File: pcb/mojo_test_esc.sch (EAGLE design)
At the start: 1 part

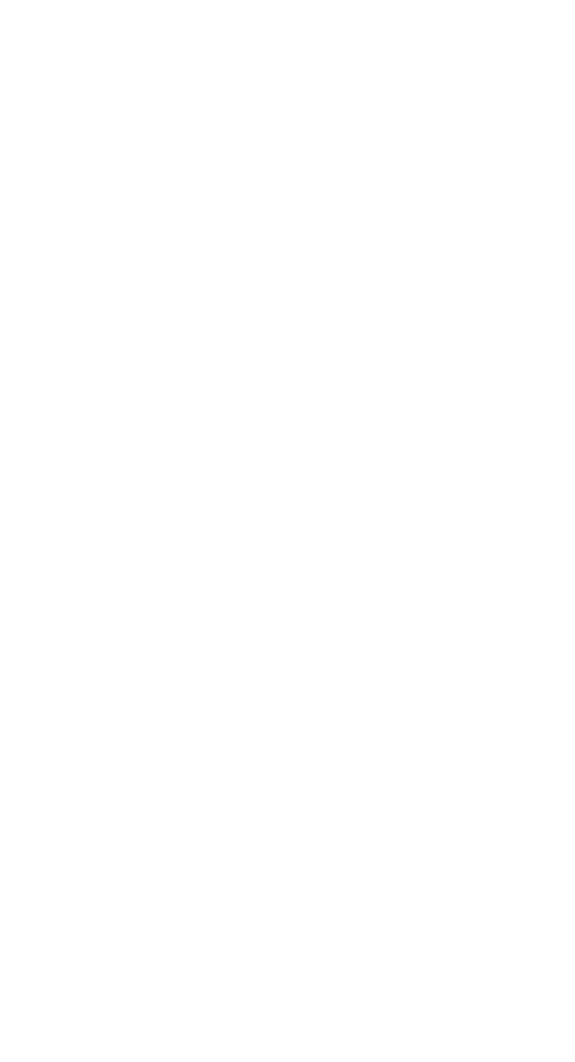
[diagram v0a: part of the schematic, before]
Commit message: Adding D2PAK mosfet to library
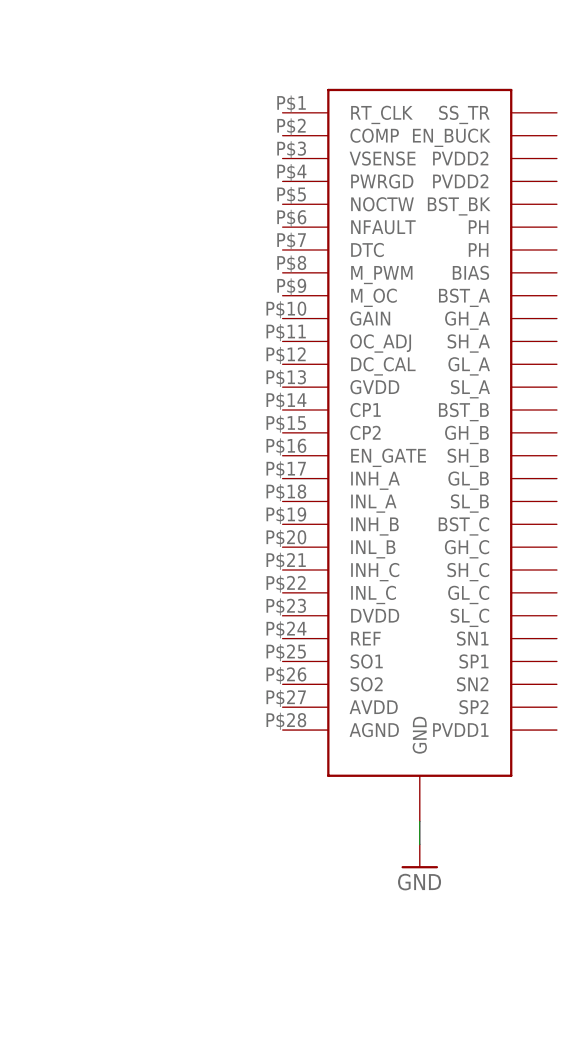
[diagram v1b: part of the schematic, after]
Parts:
- added U$1: DRV8302, mojo_test_esc:DRV8302
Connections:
- new net GND: U$1.GND
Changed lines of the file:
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@@
 <parts>
 <part name="B1" library="mojo_test_esc" deviceset="MOJO_NO_ANALOG" device="V3_NO_LABEL"/>
+<part name="U$1" library="mojo_test_esc" deviceset="DRV8302" device=""/>
+<part name="GND1" library="supply1" deviceset="GND" device=""/>
 </parts>
 <sheets>
@@
 <instance part="B1" gate="G$2" x="-27.94" y="60.96"/>
 <instance part="B1" gate="G$3" x="-27.94" y="-10.16"/>
+<instance part="U$1" gate="G$1" x="53.34" y="50.8"/>
+<instance part="GND1" gate="1" x="53.34" y="2.54"/>
 </instances>
 <busses>
 </busses>
 <nets>
+<net name="GND" class="0">
+<segment>
+<pinref part="U$1" gate="G$1" pin="GND"/>
+<pinref part="GND1" gate="1" pin="GND"/>
+<wire x1="53.34" y1="7.62" x2="53.34" y2="5.08" width="0.1524" layer="91"/>
+</segment>
+</net>
 </nets>
 </sheet>

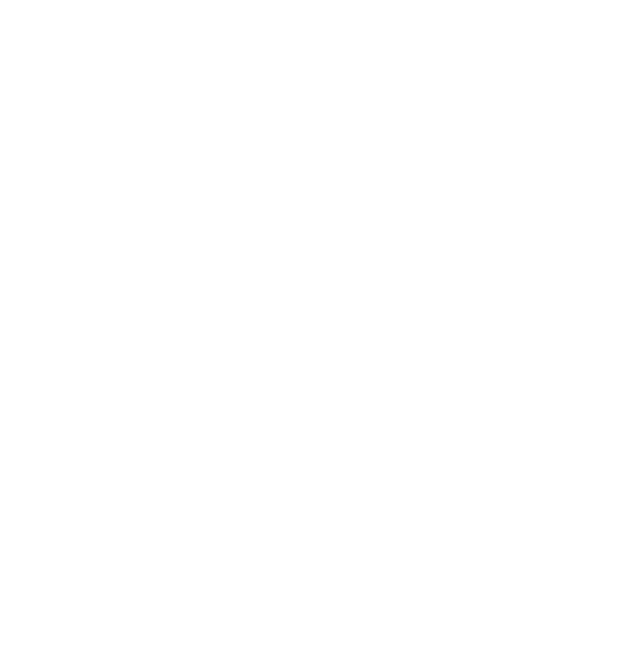
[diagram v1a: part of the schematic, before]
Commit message: Adding SOT23 mosfet packages and associated datasheet
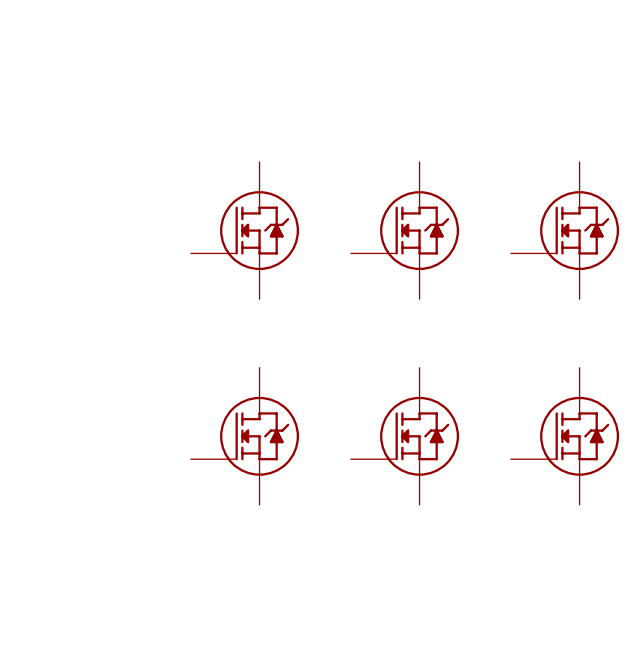
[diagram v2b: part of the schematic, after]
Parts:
- added U$2, U$3, U$4, U$5, U$6, U$7: MOSFETSOT23, mojo_test_esc:MOSFETSOT23
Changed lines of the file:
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@@
 <part name="U$1" library="mojo_test_esc" deviceset="DRV8302" device=""/>
 <part name="GND1" library="supply1" deviceset="GND" device=""/>
+<part name="U$2" library="mojo_test_esc" deviceset="MOSFET" device="SOT23"/>
+<part name="U$3" library="mojo_test_esc" deviceset="MOSFET" device="SOT23"/>
+<part name="U$4" library="mojo_test_esc" deviceset="MOSFET" device="SOT23"/>
+<part name="U$5" library="mojo_test_esc" deviceset="MOSFET" device="SOT23"/>
+<part name="U$6" library="mojo_test_esc" deviceset="MOSFET" device="SOT23"/>
+<part name="U$7" library="mojo_test_esc" deviceset="MOSFET" device="SOT23"/>
 </parts>
 <sheets>
@@
 <instance part="U$1" gate="G$1" x="53.34" y="50.8"/>
 <instance part="GND1" gate="1" x="53.34" y="2.54"/>
+<instance part="U$2" gate="G$1" x="99.06" y="66.04"/>
+<instance part="U$3" gate="G$1" x="116.84" y="66.04"/>
+<instance part="U$4" gate="G$1" x="134.62" y="66.04"/>
+<instance part="U$5" gate="G$1" x="99.06" y="43.18"/>
+<instance part="U$6" gate="G$1" x="116.84" y="43.18"/>
+<instance part="U$7" gate="G$1" x="134.62" y="43.18"/>
 </instances>
 <busses>

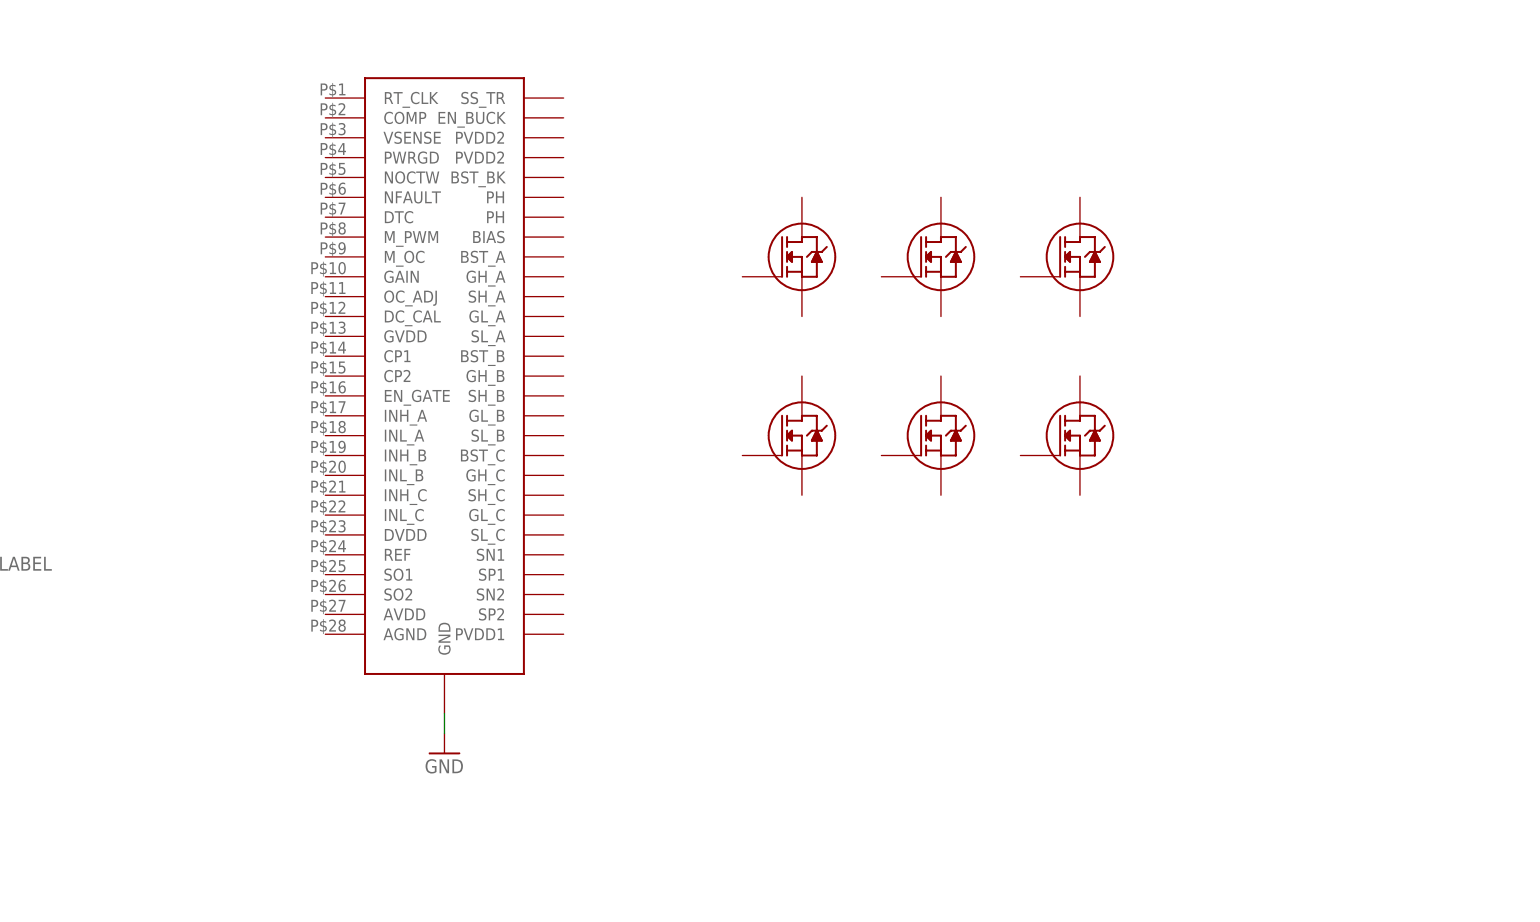
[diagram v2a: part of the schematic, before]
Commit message: Adding 8-pack resistor and updating MOSFETs again
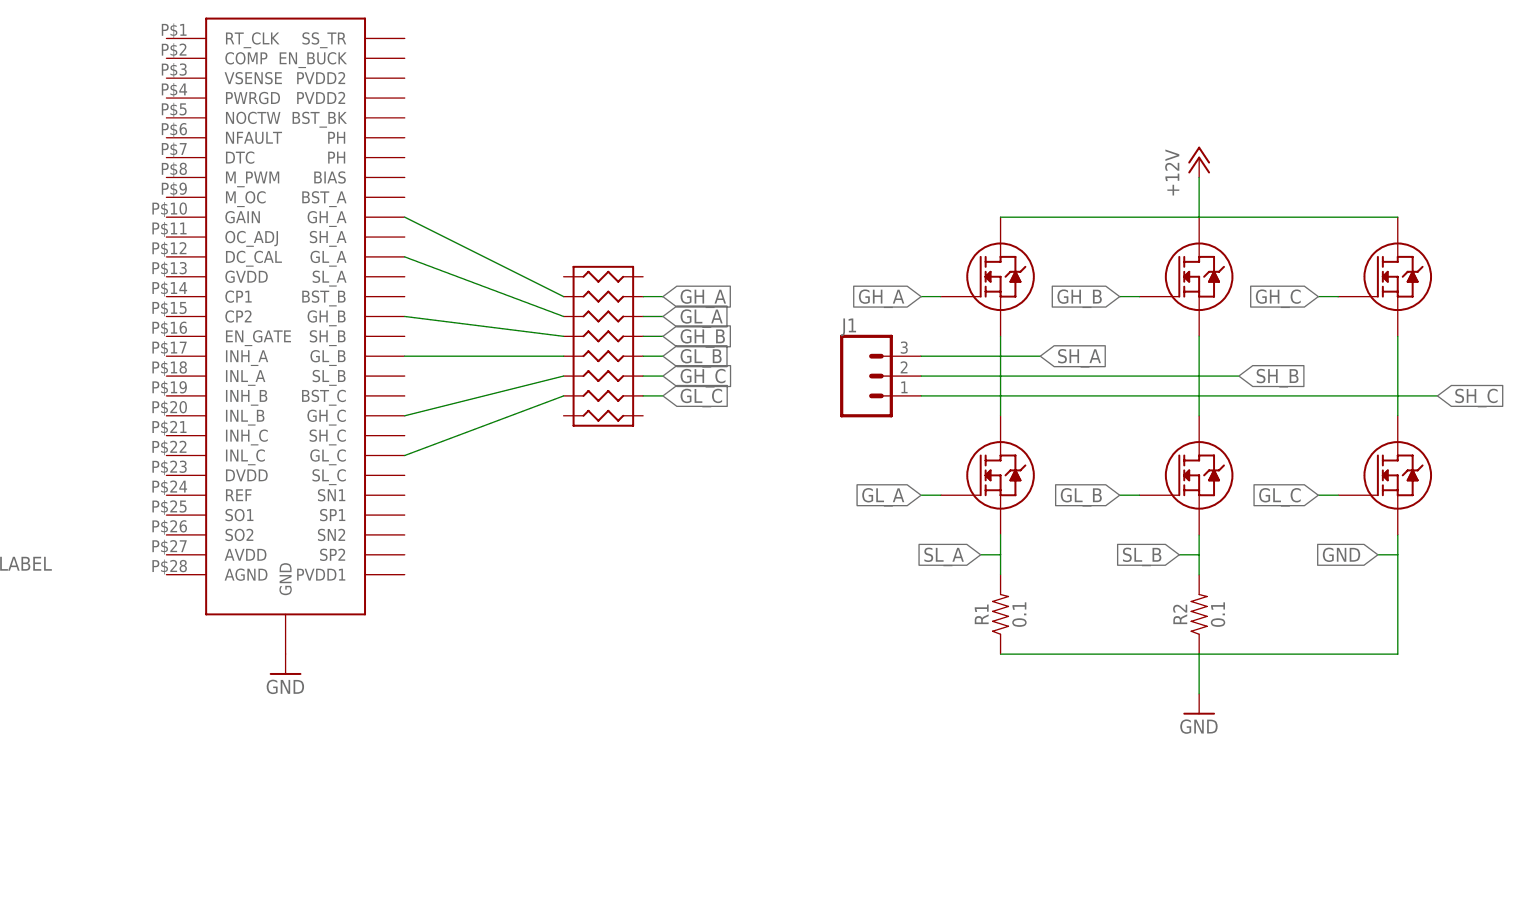
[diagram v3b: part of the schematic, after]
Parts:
- removed U$3, U$4, U$5, U$6, U$7: MOSFETSOT23, mojo_test_esc:MOSFETSOT23
- added J1: (no value), SparkFun-Connectors:CONN_03-SCREW-5MM
- added MOSFET_H_A_1, MOSFET_H_B_1, MOSFET_H_C_1, MOSFET_L_A_1, MOSFET_L_B_1, MOSFET_L_C_1: MOSFET, mojo_test_esc:MOSFET
- added R1, R2: 0.1, SparkFun-Resistors:0.1OHM-1210-1/2W-1%
- U$2: value MOSFETSOT23 -> EXB2HV; device mojo_test_esc:MOSFETSOT23 -> mojo_test_esc:EXB2HV
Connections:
- new net +12V: MOSFET_H_A_1.D2, MOSFET_H_B_1.D2, MOSFET_H_C_1.D2
- new net GH_A: MOSFET_H_A_1.G1, U$2.P2B
- new net GH_B: MOSFET_H_B_1.G1, U$2.P4B
- new net GH_C: MOSFET_H_C_1.G1, U$2.P6B
- new net GL_A: MOSFET_L_A_1.G1, U$2.P3B
- new net GL_B: MOSFET_L_B_1.G1, U$2.P5B
- new net GL_C: MOSFET_L_C_1.G1, U$2.P7B
- new net N$1: U$1.GH_A, U$2.P2
- new net N$2: U$1.GL_A, U$2.P3
- new net N$3: U$1.GH_B, U$2.P4
- new net N$4: U$1.GL_B, U$2.P5
- new net N$5: U$1.GH_C, U$2.P6
- new net N$6: U$1.GL_C, U$2.P7
- new net SH_A: J1.3, MOSFET_H_A_1.S3, MOSFET_L_A_1.D2
- new net SH_B: J1.2, MOSFET_H_B_1.S3, MOSFET_L_B_1.D2
- new net SH_C: J1.1, MOSFET_H_C_1.S3, MOSFET_L_C_1.D2
- new net SL_A: MOSFET_L_A_1.S3, R1.2
- new net SL_B: MOSFET_L_B_1.S3, R2.2
- net GND: now also MOSFET_L_C_1.S3, R1.1, R2.1
